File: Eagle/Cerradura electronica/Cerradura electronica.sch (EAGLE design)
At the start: 19 parts, among them K1 G5L, M1 ARDUINO-NANO-3.0#ISP

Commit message: Completado SCH del nuevo Hardware al 50%
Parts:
- removed D1: 1N4004, adafruit:1N4004
- removed K1: G5L, relay:G5L
- removed LED1: verde, led:LED3MM
- removed M1: ARDUINO-NANO-3.0#ISP, DIY- comercial modules:ARDUINO-NANO-3.0#ISP
- removed OK1: PC817, optocoupler:PC817
- removed R2: 10k, rcl:R-US_0204/7
- removed TECLADO: (no value), con-lstb:MA05-1
- removed X1: (no value), con-ptr500:AK500/3
- added C6, C7, C8, C9: 0.1u, rcl:C-USC0805
- added ISP: (no value), con-lstb:MA03-2
- added L1: 10u, Circuitos-Creativos-RCL:FERRITA-CHOKE
- added SV1: (no value), con-lstb:MA04-1
- added U1: ATMEGA328P_TQFP, SparkFun-DigitalIC:ATMEGA328P_TQFP
- added XT2: 8MHz, crystal:CRYSTALCTS406
- C1, C2: value 100n -> 22pF; device rcl:C-US025-025X050 -> rcl:C-USC0805
- C3, C4: value 100n -> 0.1uF; device rcl:C-US025-025X050 -> rcl:C-USC0805
- C5: value 100n -> 1uF; device rcl:C-US025-025X050 -> rcl:C-USC0805
- R1, R3, R4: device rcl:R-US_0204/7 -> rcl:R-US_R1206
- R5, R6: value 1k -> 10k; device rcl:R-US_0204/7 -> rcl:R-US_R1206
- U$1: value A5_HORIZONTAL -> A4_HORIZONTAL; device Circuitos-Creativos-Estilos:A5_HORIZONTAL -> Circuitos-Creativos-Estilos:A4_HORIZONTAL
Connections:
- removed net +12V: C5.1, D1.C, K11.1, M1.VIN, X1-1.KL
- removed net +5V: M1.5V, TECLADO.5
- removed net 1A: C3.1, M1.D6, R3.1, TECLADO.2
- removed net 2B: C4.1, M1.D5, R4.1, TECLADO.1
- removed net 3C: C1.1, M1.D8, R1.1, TECLADO.4
- removed net 4D: C2.1, M1.D7, R2.1, TECLADO.3
- removed net N$1: LED1.A, R6.2
- removed net N$2: C5.2, D1.A, K11.2, OK1.COL
- removed net N$3: OK1.A, R5.2
- removed net N$4: K12.S, X1-3.KL
- removed net RELE: M1.D3, R5.1, R6.1
- new net A0: U1.PC0(ADC0)
- new net A1: U1.PC1(ADC1)
- new net A2: U1.PC2(ADC2)
- new net A3: U1.PC3(ADC3)
- new net A6: U1.ADC6
- new net A7: U1.ADC7
- new net AREF: C4.1, U1.AREF
- new net AVCC: C5.1, L1.2, U1.AVCC
- new net D10: U1.PB2(SS/OC1B)
- new net D2: U1.PD2(INT0)
- new net D3: U1.PD3(INT1)
- new net D4: U1.PD4(XCK/T0)
- new net D5/2: C7.1, R4.1, U1.PD5(T1)
- new net D6/1: C6.1, R3.1, U1.PD6(AIN0)
- new net D7/4: C9.1, R6.1, U1.PD7(AIN1)
- new net D8/3: C8.1, R5.1, U1.PB0(ICP)
- new net D9: U1.PB1(OC1A)
- new net MISO: ISP.4, U1.PB4(MISO)
- new net MOSI: ISP.6, U1.PB3(MOSI/OC2)
- new net OS1: C1.1, U1.PB6(XTAL1/TOSC1), XT2.2
- new net OS2: C2.1, U1.PB7(XTAL2/TOSC2), XT2.1
- new net RST: ISP.3, R1.2, U1.PC6(/RESET)
- new net RX1: SV1.3, U1.PD0(RXD)
- new net SCK: ISP.2, U1.PB5(SCK)
- new net TX0: SV1.2, U1.PD1(TXD)
- new net VCC: C3.1, ISP.5, L1.1, R1.1, SV1.1, U1.VCC@4, U1.VCC@6
- net GND: now also C5.2, C6.2, C7.2, C8.2, C9.2, ISP.1, R5.2, R6.2, SV1.4, U1.AGND, U1.GND@3, U1.GND@5; no longer K12.P, LED1.C, M1.GND.1, OK1.C, OK1.EMIT, R1.2, R2.2, X1-2.KL
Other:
- note added: "1"
- note added: "1.1"
- note added: "ENTRADAS TECLADO 4x1"
- note added: "MCU ATMEGA328P-AU"
- moved on the sheet: C1, C2, C3, C4, C5, R1, R3, R4, R5, R6

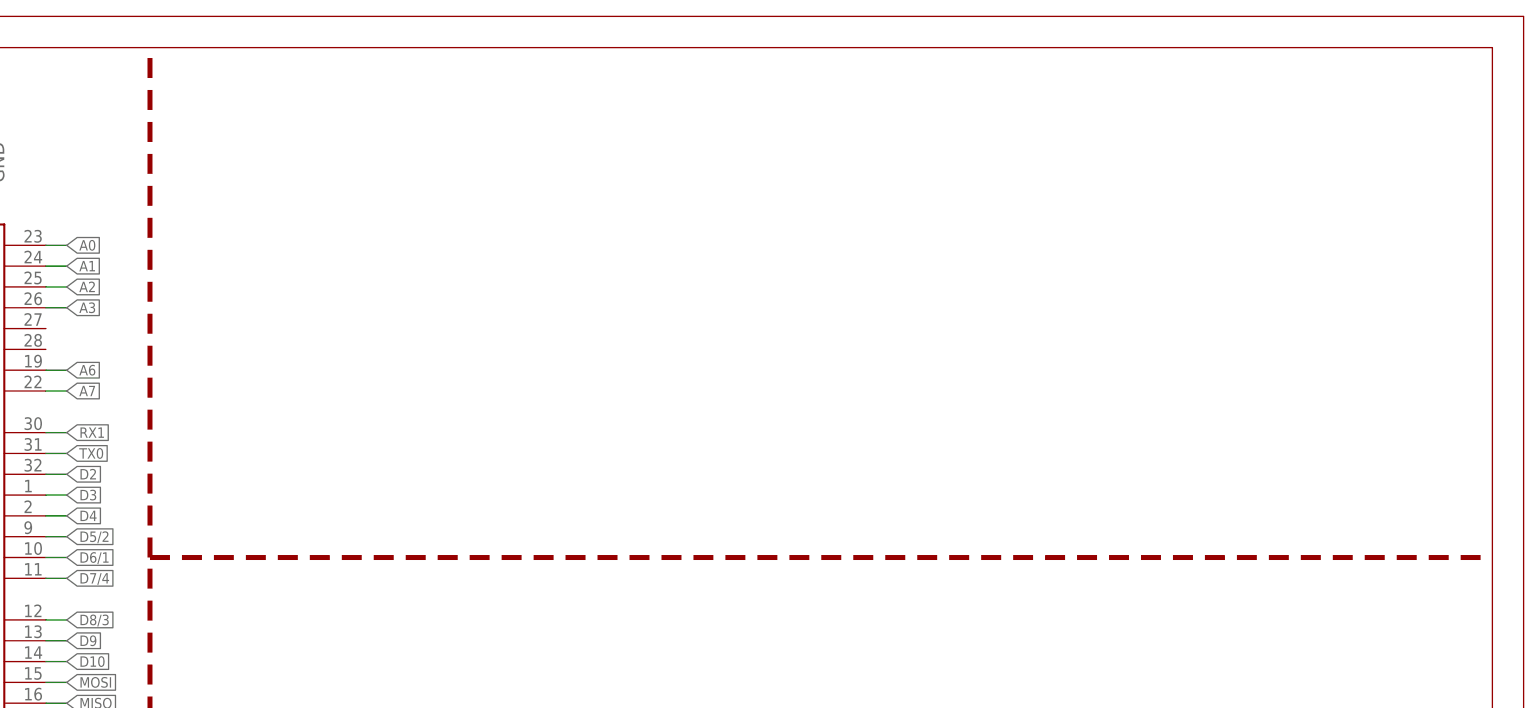
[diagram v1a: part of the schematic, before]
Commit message: Terminado regulador 5V y etapa de potencia
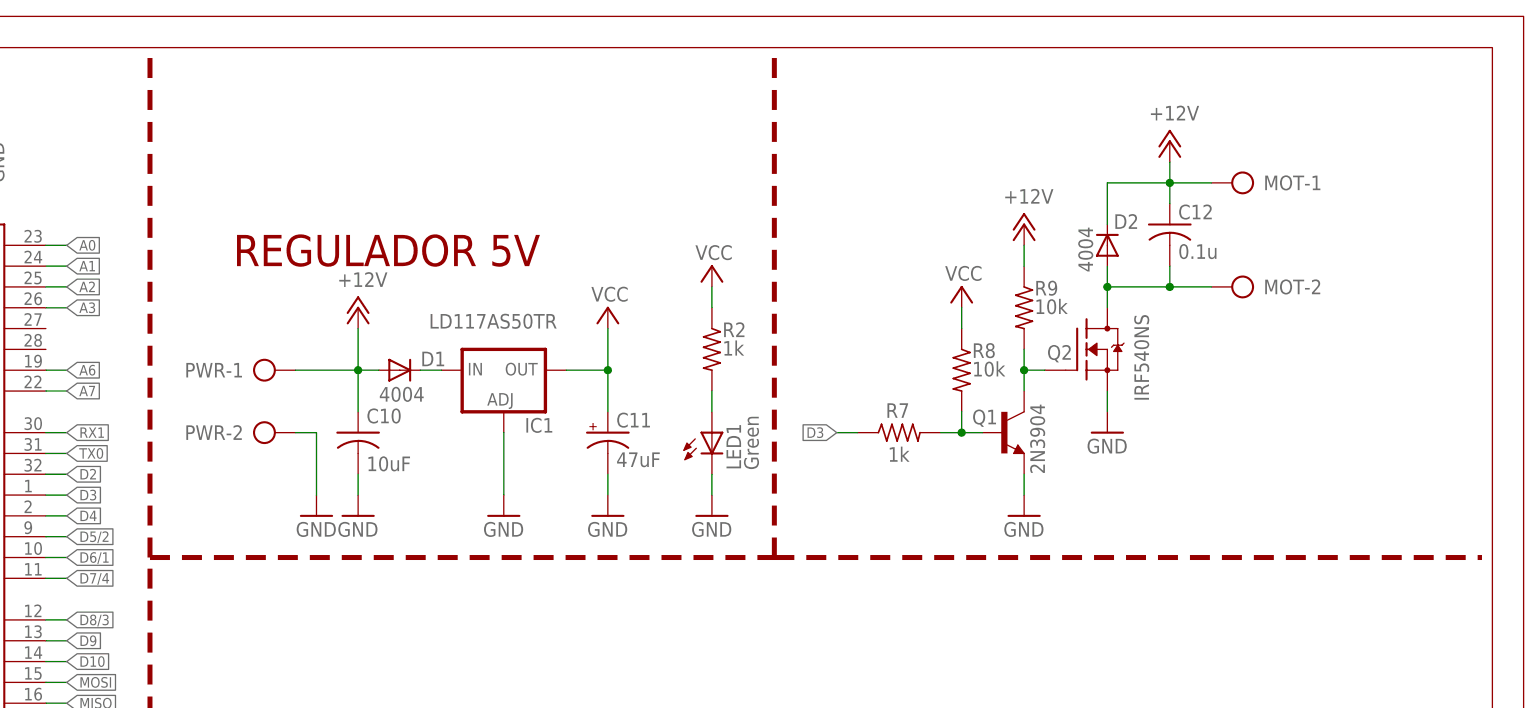
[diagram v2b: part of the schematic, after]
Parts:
- added C10: 10uF, rcl:C-USC0805
- added C11: 47uF, rcl:CPOL-USR/2012-12W
- added C12: 0.1u, rcl:C-USC0805
- added D1, D2: 4004, diode:DIODE-DO214AC
- added IC1: LD117AS50TR, v-reg:LD117AS50TR
- added LED1: Green, led:LEDCHIPLED_0805
- added MOT, PWR: (no value), con-ptr500:AK500/2
- added Q1: 2N3904, transistor:MMBT3904LT1-NPN-SOT23-BEC
- added Q2: IRF540NS, Circuitos-Creativos-Transistores:IRF540NS
- added R2, R7: 1k, rcl:R-US_R1206
- added R8, R9: 10k, rcl:R-US_R1206
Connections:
- new net +12V: C10.1, C12.1, D1.A, D2.C, MOT-1.KL, PWR-1.KL, R9.1
- new net N$1: LED1.A, R2.2
- new net N$2: Q1.B, R7.2, R8.2
- new net N$3: D1.C, IC1.IN
- new net N$4: Q1.C, Q2.G, R9.2
- new net N$5: C12.2, D2.A, MOT-2.KL, Q2.D
- net D3: now also R7.1
- net GND: now also C10.2, C11.-, IC1.ADJ, LED1.C, PWR-2.KL, Q1.E, Q2.S
- net VCC: now also C11.+, IC1.OUT, R2.1, R8.1
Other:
- note added: "REGULADOR 5V"

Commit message: Terminado el SCH, inicio del BRD
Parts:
- added R10: 10k, rcl:R-US_R1206
- added S1: Reset, Testing:SWITCH-MOMENTARY-2-SMD-1101NE
- added TECLADO: (no value), con-lstb:MA07-1
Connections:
- removed net N$5: C12.2, D2.A, MOT-2.KL, Q2.D
- new net MOT_ON: C12.2, D2.A, MOT-2.KL, Q2.D, TECLADO.2
- new net N$11: R10.2, TECLADO.1
- new net RESET: R1.2, S1.2, U1.PC6(/RESET)
- net +12V: now also R10.1
- net D5/2: now also TECLADO.7
- net D6/1: now also TECLADO.6
- net D7/4: now also TECLADO.5
- net D8/3: now also TECLADO.4
- net GND: now also S1.1
- net OS1: now also U1.PB6(XTAL1); no longer U1.PB6(XTAL1/TOSC1)
- net OS2: now also U1.PB7(XTAL2); no longer U1.PB7(XTAL2/TOSC2)
- net RST: no longer R1.2, U1.PC6(/RESET)
- net VCC: now also TECLADO.3
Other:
- note added: "CONECTOR PCB TECLADO"
- note added: "ETAPA DE POTENCIA MOSFET"
- moved on the sheet: C1, C10, C11, C12, C2, C3, C4, D1, D2, IC1, ISP, LED1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

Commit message: Componentes ubicados, inicio ruteo
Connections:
- removed net RESET: R1.2, S1.2, U1.PC6(/RESET)
- net +12V: now also PWR-2.KL; no longer PWR-1.KL
- net GND: now also PWR-1.KL; no longer PWR-2.KL
- net RST: now also R1.2, S1.2, U1.PC6(/RESET)
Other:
- moved on the sheet: PWR-1, PWR-2, R1, S1
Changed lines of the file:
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@@
 <attribute name="VALUE" x="10.16" y="99.06" size="1.778" layer="96" ratio="10" rot="R180"/>
 </instance>
-<instance part="P+4" gate="VCC" x="7.62" y="162.56" smashed="yes">
-<attribute name="VALUE" x="10.16" y="165.1" size="1.778" layer="96" ratio="10" rot="R180"/>
-</instance>
-<instance part="R1" gate="G$1" x="7.62" y="152.4" smashed="yes" rot="R270">
-<attribute name="NAME" x="8.89" y="153.8986" size="1.778" layer="95" ratio="10"/>
-<attribute name="VALUE" x="8.89" y="151.638" size="1.778" layer="96" ratio="10"/>
+<instance part="P+4" gate="VCC" x="10.16" y="162.56" smashed="yes">
+<attribute name="VALUE" x="12.7" y="165.1" size="1.778" layer="96" ratio="10" rot="R180"/>
+</instance>
+<instance part="R1" gate="G$1" x="10.16" y="152.4" smashed="yes" rot="R270">
+<attribute name="NAME" x="11.43" y="153.8986" size="1.778" layer="95" ratio="10"/>
+<attribute name="VALUE" x="11.43" y="151.638" size="1.778" layer="96" ratio="10"/>
 </instance>
 <instance part="P+18" gate="VCC" x="17.78" y="134.62" smashed="yes" rot="R90">
@@
 <attribute name="VALUE" x="158.75" y="154.178" size="1.778" layer="96" ratio="10"/>
 </instance>
-<instance part="PWR" gate="-1" x="101.6" y="152.4"/>
-<instance part="PWR" gate="-2" x="101.6" y="144.78"/>
+<instance part="PWR" gate="-1" x="101.6" y="144.78"/>
+<instance part="PWR" gate="-2" x="101.6" y="152.4"/>
 <instance part="C11" gate="G$1" x="144.78" y="144.78" smashed="yes">
 <attribute name="NAME" x="145.796" y="145.415" size="1.778" layer="95" ratio="10"/>
@@
 <attribute name="VALUE" x="116.84" y="119.38" size="1.778" layer="96" ratio="10" rot="R180"/>
 </instance>
-<instance part="GND17" gate="1" x="7.62" y="127"/>
-<instance part="S1" gate="G$1" x="7.62" y="137.16" rot="R90"/>
+<instance part="GND17" gate="1" x="10.16" y="127"/>
+<instance part="S1" gate="G$1" x="10.16" y="137.16" rot="R90"/>
 </instances>
 <busses>
@@
 <segment>
 <pinref part="GND14" gate="1" pin="GND"/>
+<wire x1="109.22" y1="144.78" x2="109.22" y2="137.16" width="0.1524" layer="91"/>
+<pinref part="PWR" gate="-1" pin="KL"/>
 <wire x1="106.68" y1="144.78" x2="109.22" y2="144.78" width="0.1524" layer="91"/>
-<wire x1="109.22" y1="144.78" x2="109.22" y2="137.16" width="0.1524" layer="91"/>
-<pinref part="PWR" gate="-2" pin="KL"/>
 </segment>
 <segment>
@@
 </segment>
 <segment>
-<wire x1="7.62" y1="132.08" x2="7.62" y2="129.54" width="0.1524" layer="91"/>
+<wire x1="10.16" y1="132.08" x2="10.16" y2="129.54" width="0.1524" layer="91"/>
 <pinref part="GND17" gate="1" pin="GND"/>
 <pinref part="S1" gate="G$1" pin="1"/>
@@
 <pinref part="R1" gate="G$1" pin="1"/>
 <pinref part="P+4" gate="VCC" pin="VCC"/>
-<wire x1="7.62" y1="157.48" x2="7.62" y2="160.02" width="0.1524" layer="91"/>
+<wire x1="10.16" y1="157.48" x2="10.16" y2="160.02" width="0.1524" layer="91"/>
 </segment>
 <segment>
@@
 <wire x1="43.18" y1="66.04" x2="33.02" y2="66.04" width="0.1524" layer="91"/>
 </segment>
+<segment>
+<wire x1="10.16" y1="142.24" x2="10.16" y2="144.78" width="0.1524" layer="91"/>
+<pinref part="S1" gate="G$1" pin="2"/>
+<pinref part="U1" gate="U$1" pin="PC6(/RESET)"/>
+<wire x1="27.94" y1="144.78" x2="10.16" y2="144.78" width="0.1524" layer="91"/>
+<pinref part="R1" gate="G$1" pin="2"/>
+<wire x1="10.16" y1="147.32" x2="10.16" y2="144.78" width="0.1524" layer="91"/>
+<junction x="10.16" y="144.78"/>
+<wire x1="10.16" y1="144.78" x2="7.62" y2="144.78" width="0.1524" layer="91"/>
+<label x="7.62" y="144.78" size="1.27" layer="95" ratio="10" rot="R180" xref="yes"/>
+</segment>
 </net>
 <net name="D6/1" class="0">
@@
 <pinref part="P+17" gate="1" pin="+12V"/>
 <wire x1="114.3" y1="157.48" x2="114.3" y2="152.4" width="0.1524" layer="91"/>
-<pinref part="PWR" gate="-1" pin="KL"/>
-<wire x1="114.3" y1="152.4" x2="106.68" y2="152.4" width="0.1524" layer="91"/>
 <pinref part="D1" gate="G$1" pin="A"/>
 <wire x1="116.84" y1="152.4" x2="114.3" y2="152.4" width="0.1524" layer="91"/>
+<pinref part="PWR" gate="-2" pin="KL"/>
+<wire x1="106.68" y1="152.4" x2="114.3" y2="152.4" width="0.1524" layer="91"/>
 </segment>
 <segment>
@@
 </segment>
 </net>
-<net name="RESET" class="0">
-<segment>
-<wire x1="7.62" y1="142.24" x2="7.62" y2="144.78" width="0.1524" layer="91"/>
-<pinref part="S1" gate="G$1" pin="2"/>
-<pinref part="U1" gate="U$1" pin="PC6(/RESET)"/>
-<wire x1="27.94" y1="144.78" x2="7.62" y2="144.78" width="0.1524" layer="91"/>
-<pinref part="R1" gate="G$1" pin="2"/>
-<wire x1="7.62" y1="147.32" x2="7.62" y2="144.78" width="0.1524" layer="91"/>
-<junction x="7.62" y="144.78"/>
-</segment>
-</net>

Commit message: Cambio solicitado por Segcontrol SAS
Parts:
- C10: device rcl:C-USC0805 -> rcl:C-USC1206
- C11: device rcl:CPOL-USR/2012-12W -> rcl:C-USC1206
- R10: value 10k -> 1k
- XT2: device crystal:CRYSTALCTS406 -> crystal:CRYSTALSM49
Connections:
- net +12V: no longer R10.1
- net GND: now also C11.2, TECLADO.2; no longer C11.-
- net MOT_ON: no longer TECLADO.2
- net VCC: now also C11.1, R10.1; no longer C11.+
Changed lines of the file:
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@@
 <setting verticaltext="up"/>
 </settings>
-<grid distance="0.1" unitdist="inch" unit="inch" style="lines" multiple="1" display="yes" altdistance="0.01" altunitdist="inch" altunit="inch"/>
+<grid distance="0.1" unitdist="inch" unit="inch" style="lines" multiple="1" display="no" altdistance="0.01" altunitdist="inch" altunit="inch"/>
 <layers>
 <layer number="1" name="Top" color="4" fill="1" visible="yes" active="no"/>
@@
 <part name="C3" library="rcl" deviceset="C-US" device="C0805" value="0.1uF"/>
 <part name="C4" library="rcl" deviceset="C-US" device="C0805" value="0.1uF"/>
-<part name="XT2" library="crystal" deviceset="CRYSTAL" device="CTS406" value="8MHz"/>
+<part name="XT2" library="crystal" deviceset="CRYSTAL" device="SM49" value="8MHz"/>
 <part name="C1" library="rcl" deviceset="C-US" device="C0805" value="22pF"/>
 <part name="C2" library="rcl" deviceset="C-US" device="C0805" value="22pF"/>
@@
 <part name="IC1" library="v-reg" deviceset="LD117A?*" device="S" technology="50TR" value="LD117AS50TR"/>
 <part name="GND14" library="supply1" deviceset="GND" device=""/>
-<part name="C10" library="rcl" deviceset="C-US" device="C0805" value="10uF"/>
+<part name="C10" library="rcl" deviceset="C-US" device="C1206" value="10uF"/>
 <part name="GND19" library="supply1" deviceset="GND" device=""/>
 <part name="GND20" library="supply1" deviceset="GND" device=""/>
@@
 <part name="R2" library="rcl" deviceset="R-US_" device="R1206" value="1k"/>
 <part name="PWR" library="con-ptr500" deviceset="AK500/2" device=""/>
-<part name="C11" library="rcl" deviceset="CPOL-US" device="R/2012-12W" value="47uF"/>
 <part name="R7" library="rcl" deviceset="R-US_" device="R1206" value="1k"/>
 <part name="R8" library="rcl" deviceset="R-US_" device="R1206" value="10k"/>
@@
 <part name="P+3" library="supply1" deviceset="+12V" device=""/>
 <part name="TECLADO" library="con-lstb" deviceset="MA07-1" device=""/>
-<part name="R10" library="rcl" deviceset="R-US_" device="R1206" value="10k"/>
-<part name="P+5" library="supply1" deviceset="+12V" device=""/>
+<part name="R10" library="rcl" deviceset="R-US_" device="R1206" value="1k"/>
 <part name="P+6" library="supply1" deviceset="VCC" device=""/>
 <part name="GND17" library="SparkFun" deviceset="GND" device=""/>
 <part name="S1" library="Testing" deviceset="SWITCH-MOMENTARY-2" device="-SMD-1101NE" value="Reset"/>
+<part name="P+5" library="supply1" deviceset="VCC" device=""/>
+<part name="GND18" library="supply1" deviceset="GND" device=""/>
+<part name="C11" library="rcl" deviceset="C-US" device="C1206" value="47uF"/>
 </parts>
 <sheets>
@@
 <instance part="PWR" gate="-1" x="101.6" y="144.78"/>
 <instance part="PWR" gate="-2" x="101.6" y="152.4"/>
-<instance part="C11" gate="G$1" x="144.78" y="144.78" smashed="yes">
-<attribute name="NAME" x="145.796" y="145.415" size="1.778" layer="95" ratio="10"/>
-<attribute name="VALUE" x="145.796" y="140.589" size="1.778" layer="96" ratio="10"/>
-</instance>
 <instance part="R7" gate="G$1" x="185.42" y="119.38" smashed="yes">
 <attribute name="NAME" x="186.69" y="122.9614" size="1.778" layer="95" ratio="10" rot="R180"/>
@@
 <attribute name="VALUE" x="120.65" y="113.538" size="1.778" layer="96" ratio="10"/>
 </instance>
-<instance part="P+5" gate="1" x="119.38" y="124.46" smashed="yes">
-<attribute name="VALUE" x="116.84" y="127" size="1.778" layer="96" ratio="10"/>
-</instance>
 <instance part="P+6" gate="VCC" x="114.3" y="116.84" smashed="yes">
 <attribute name="VALUE" x="116.84" y="119.38" size="1.778" layer="96" ratio="10" rot="R180"/>
@@
 <instance part="GND17" gate="1" x="10.16" y="127"/>
 <instance part="S1" gate="G$1" x="10.16" y="137.16" rot="R90"/>
+<instance part="P+5" gate="VCC" x="119.38" y="124.46" smashed="yes">
+<attribute name="VALUE" x="121.92" y="127" size="1.778" layer="96" ratio="10" rot="R180"/>
+</instance>
+<instance part="GND18" gate="1" x="106.68" y="109.22" smashed="yes" rot="R90">
+<attribute name="VALUE" x="109.22" y="106.68" size="1.778" layer="96" ratio="10" rot="R90"/>
+</instance>
+<instance part="C11" gate="G$1" x="144.78" y="144.78" smashed="yes">
+<attribute name="NAME" x="145.796" y="145.923" size="1.778" layer="95" ratio="10"/>
+<attribute name="VALUE" x="145.796" y="140.081" size="1.778" layer="96" ratio="10"/>
+</instance>
 </instances>
 <busses>
@@
 <pinref part="GND21" gate="1" pin="GND"/>
 <wire x1="144.78" y1="139.7" x2="144.78" y2="137.16" width="0.1524" layer="91"/>
-<pinref part="C11" gate="G$1" pin="-"/>
+<pinref part="C11" gate="G$1" pin="2"/>
 </segment>
 <segment>
@@
 <pinref part="GND17" gate="1" pin="GND"/>
 <pinref part="S1" gate="G$1" pin="1"/>
+</segment>
+<segment>
+<pinref part="TECLADO" gate="1" pin="2"/>
+<wire x1="101.6" y1="109.22" x2="104.14" y2="109.22" width="0.1524" layer="91"/>
+<pinref part="GND18" gate="1" pin="GND"/>
 </segment>
 </net>
@@
 <wire x1="144.78" y1="152.4" x2="144.78" y2="147.32" width="0.1524" layer="91"/>
 <junction x="144.78" y="152.4"/>
-<pinref part="C11" gate="G$1" pin="+"/>
+<pinref part="C11" gate="G$1" pin="1"/>
 </segment>
 <segment>
@@
 <wire x1="101.6" y1="111.76" x2="114.3" y2="111.76" width="0.1524" layer="91"/>
 <wire x1="114.3" y1="111.76" x2="114.3" y2="114.3" width="0.1524" layer="91"/>
+</segment>
+<segment>
+<pinref part="R10" gate="G$1" pin="1"/>
+<wire x1="119.38" y1="121.92" x2="119.38" y2="119.38" width="0.1524" layer="91"/>
+<pinref part="P+5" gate="VCC" pin="VCC"/>
 </segment>
 </net>
@@
 <pinref part="P+3" gate="1" pin="+12V"/>
 <wire x1="218.44" y1="149.86" x2="218.44" y2="152.4" width="0.1524" layer="91"/>
-</segment>
-<segment>
-<pinref part="R10" gate="G$1" pin="1"/>
-<pinref part="P+5" gate="1" pin="+12V"/>
-<wire x1="119.38" y1="121.92" x2="119.38" y2="119.38" width="0.1524" layer="91"/>
 </segment>
 </net>
@@
 <label x="220.98" y="132.08" size="1.27" layer="95" ratio="10" xref="yes"/>
 </segment>
-<segment>
-<pinref part="TECLADO" gate="1" pin="2"/>
-<wire x1="101.6" y1="109.22" x2="104.14" y2="109.22" width="0.1524" layer="91"/>
-<label x="104.14" y="109.22" size="1.27" layer="95" ratio="10" xref="yes"/>
-</segment>
-</net>
+</net>
